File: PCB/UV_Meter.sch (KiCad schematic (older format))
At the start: 11 parts, among them SW1 SW_Push, U1 ATtiny85-20PU

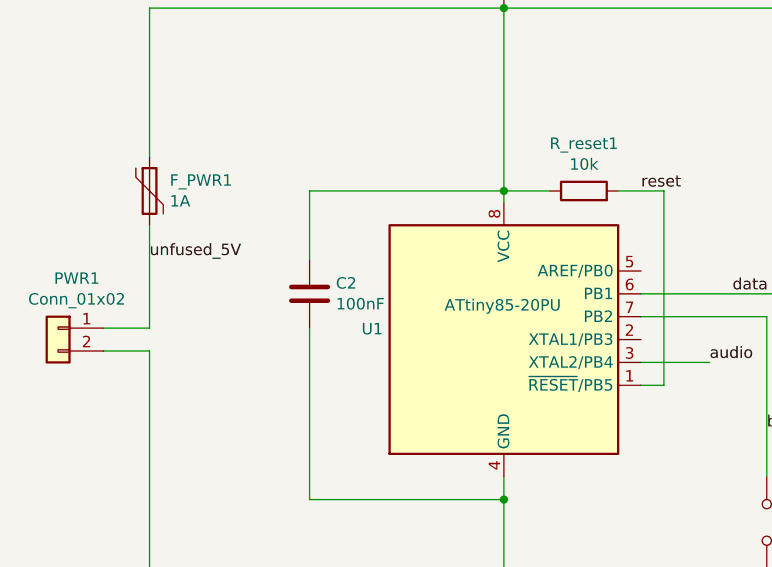
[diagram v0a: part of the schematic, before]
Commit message: improve label placement
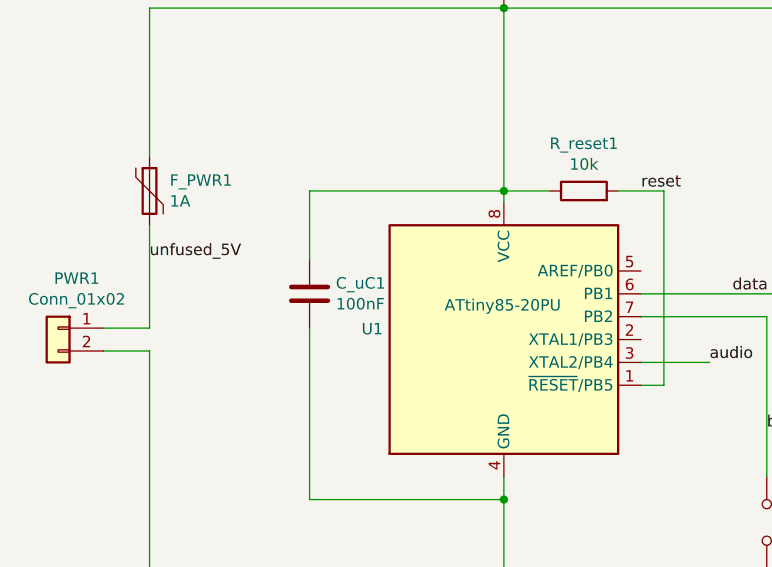
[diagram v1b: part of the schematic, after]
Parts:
- renumbered C2 to C_uC1
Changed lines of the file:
@@
 	2750 1250 2750 2050
 $Comp
-L Device:C C2
+L Device:C C_uC1
 U 1 1 5CC2270E
 P 1900 2500
-F 0 "C2" H 2015 2546 50  0000 L CNN
+F 0 "C_uC1" H 2015 2546 50  0000 L CNN
 F 1 "100nF" H 2015 2455 50  0000 L CNN
 F 2 "Capacitor_SMD:C_0603_1608Metric" H 1938 2350 50  0001 C CNN
